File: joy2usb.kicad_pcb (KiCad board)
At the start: 2 copper layers, 55 x 90 mm, 18 parts, among them J1 DB9_Male, J2 Conn_02x04_Odd_Even, SW1 RST, SW2 SW_SPDT, U1 Arduino_Pro_Micro, U2 4066

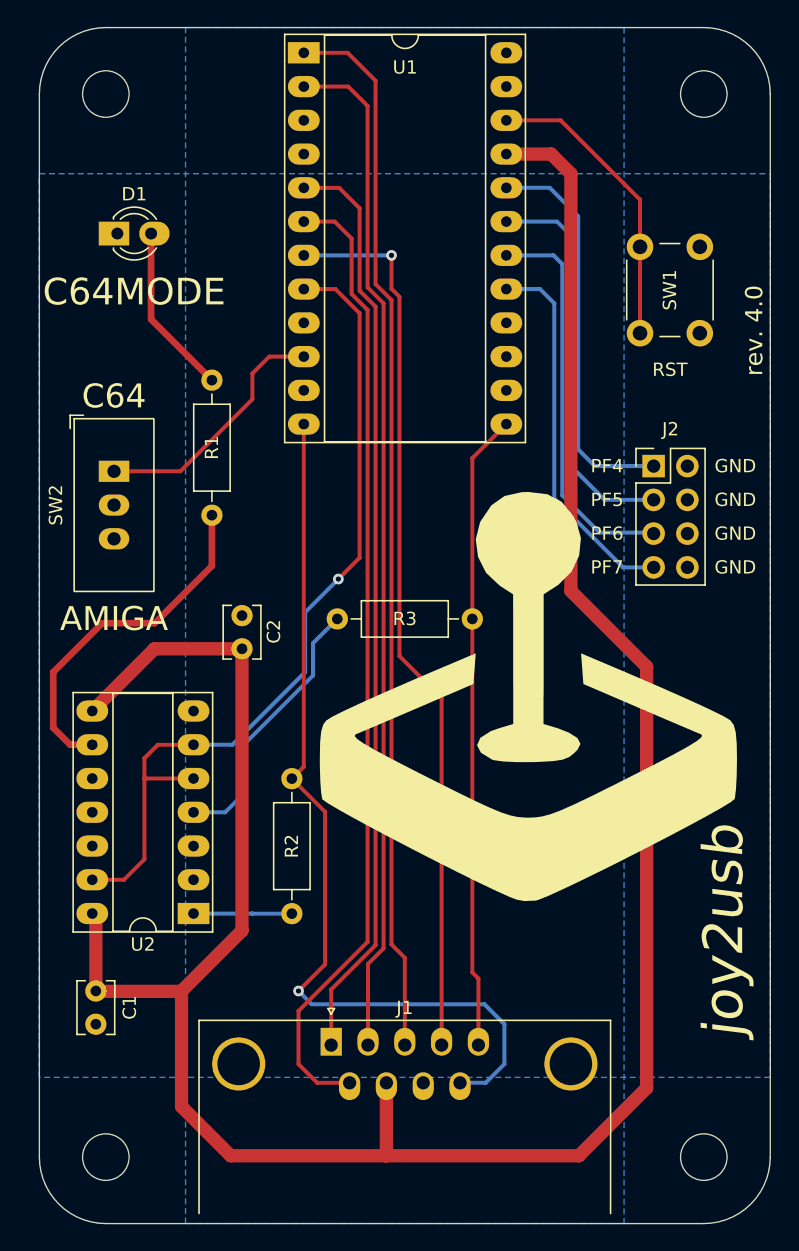
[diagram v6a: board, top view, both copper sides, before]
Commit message: PCB Rev. 4.1
SW2 minor amendment
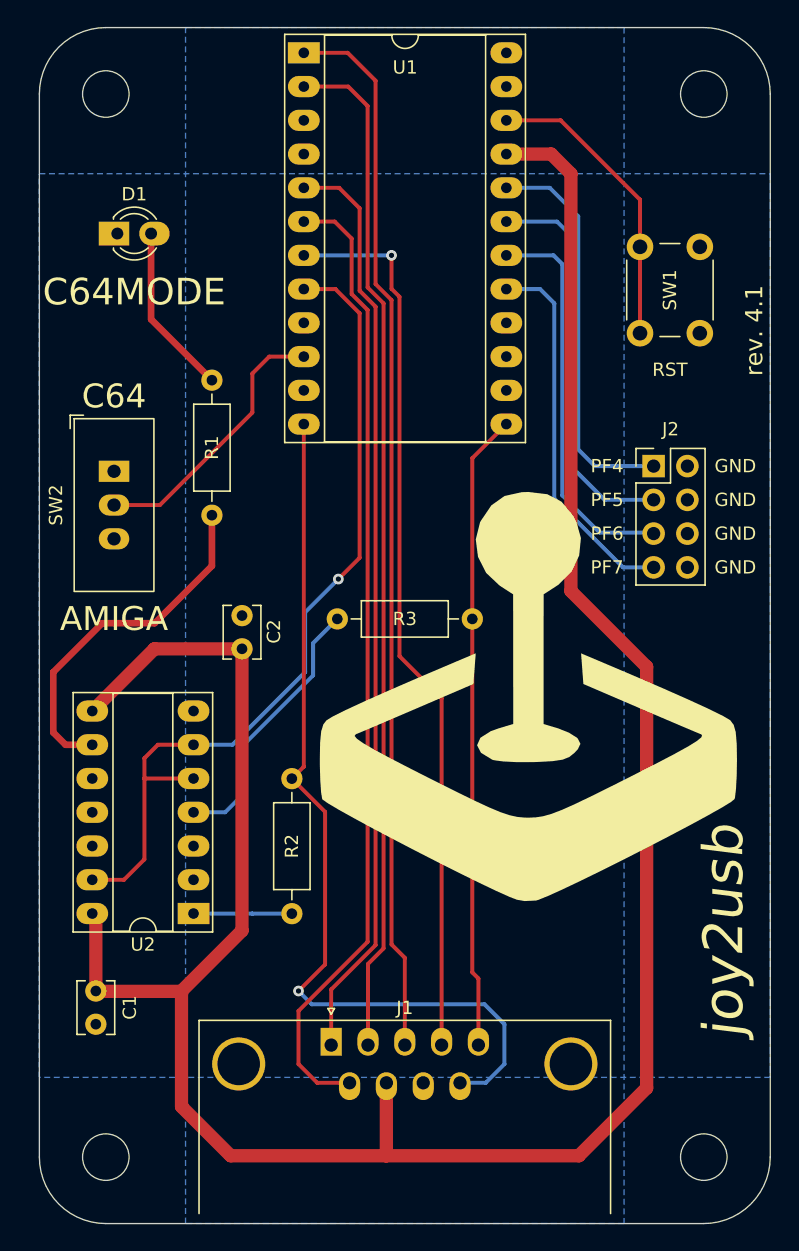
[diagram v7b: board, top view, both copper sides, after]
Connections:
- SW2 pad 1: Net-(SW2-Pad1) -> GND
- SW2 pad 2: GND -> Net-(SW2-Pad2)
- SW2 pad 3: GND -> unconnected-(SW2-Pad3)
- U1 pad 10: Net-(SW2-Pad1) -> Net-(SW2-Pad2)
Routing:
- net Net-(SW2-Pad2): track 0.00 -> 20.6 mm
- net Net-(SW2-Pad1): track 19.0 -> 0.00 mm
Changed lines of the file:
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@@
   (title_block
     (title "joy2usb")
-    (rev "4.0")
+    (rev "4.1")
     (company "mistepien")
   )
@@
   (net 20 "/PF4")
   (net 21 "Net-(D1-Pad2)")
-  (net 22 "Net-(SW2-Pad1)")
+  (net 22 "Net-(SW2-Pad2)")
   (net 23 "/F2F3MODE")
   (net 24 "Net-(R1-Pad1)")
   (net 25 "Net-(R2-Pad2)")
   (net 26 "Net-(R3-Pad1)")
+  (net 27 "unconnected-(SW2-Pad3)")
   (footprint "Resistor_THT:R_Axial_DIN0207_L6.3mm_D2.5mm_P10.16mm_Horizontal" (layer "F.Cu")
     (at 135.42 99.5)
@@
     (fp_line (start -1.27 12.45) (end 1.27 12.45) (layer "F.Fab") (width 0.1))
     (pad "1" thru_hole rect (at 0 8.27) (size 2.3 1.6) (drill 1) (layers *.Cu *.Mask)
-      (net 22 "Net-(SW2-Pad1)") (pinfunction "A") (pintype "passive"))
+      (net 8 "GND") (pinfunction "A") (pintype "passive"))
     (pad "2" thru_hole oval (at 0 10.81) (size 2.3 1.6) (drill 1) (layers *.Cu *.Mask)
-      (net 8 "GND") (pinfunction "B") (pintype "passive"))
+      (net 22 "Net-(SW2-Pad2)") (pinfunction "B") (pintype "passive"))
     (pad "3" thru_hole oval (at 0 13.35) (size 2.3 1.6) (drill 1) (layers *.Cu *.Mask)
-      (net 8 "GND") (pinfunction "C") (pintype "passive"))
+      (net 27 "unconnected-(SW2-Pad3)") (pinfunction "C") (pintype "passive+no_connect"))
   )
   (footprint "Capacitor_THT:C_Disc_D3.8mm_W2.6mm_P2.50mm" (layer "F.Cu")
@@
       (net 14 "unconnected-(U1-Pad9)") (pinfunction "Digital6/PD7") (pintype "bidirectional+no_connect"))
     (pad "10" thru_hole oval locked (at 0 22.86) (size 2.4 1.6) (drill 0.8) (layers *.Cu *.Mask)
-      (net 22 "Net-(SW2-Pad1)") (pinfunction "Digital7/PE6") (pintype "bidirectional"))
+      (net 22 "Net-(SW2-Pad2)") (pinfunction "Digital7/PE6") (pintype "bidirectional"))
     (pad "11" thru_hole oval locked (at 0 25.4) (size 2.4 1.6) (drill 0.8) (layers *.Cu *.Mask)
       (net 12 "unconnected-(U1-Pad11)") (pinfunction "Digital8/PB4") (pintype "bidirectional+no_connect"))
@@
   (segment (start 121.407 76.957) (end 121.407 70.5) (width 0.5) (layer "F.Cu") (net 21))
   (segment (start 125.984 81.534) (end 121.407 76.957) (width 0.5) (layer "F.Cu") (net 21))
-  (segment (start 123.608 88.392) (end 129.03 82.97) (width 0.3) (layer "F.Cu") (net 22))
   (segment (start 130.3 79.76) (end 132.9 79.76) (width 0.3) (layer "F.Cu") (net 22))
-  (segment (start 129.03 82.97) (end 129.03 81.03) (width 0.3) (layer "F.Cu") (net 22))
+  (segment (start 118.618 90.932) (end 122.068 90.932) (width 0.3) (layer "F.Cu") (net 22))
   (segment (start 129.03 81.03) (end 130.3 79.76) (width 0.3) (layer "F.Cu") (net 22))
-  (segment (start 118.618 88.392) (end 123.608 88.392) (width 0.3) (layer "F.Cu") (net 22))
+  (segment (start 129.03 83.97) (end 129.03 81.03) (width 0.3) (layer "F.Cu") (net 22))
+  (segment (start 122.068 90.932) (end 129.03 83.97) (width 0.3) (layer "F.Cu") (net 22))
   (segment (start 120.904 109.982) (end 121.915 108.971) (width 0.3) (layer "F.Cu") (net 23))
   (segment (start 120.909 111.511) (end 120.904 111.506) (width 0.3) (layer "F.Cu") (net 23))
@@
   (segment (start 133 103.5) (end 127.534 108.966) (width 0.3) (layer "B.Cu") (net 23))
   (segment (start 133 99) (end 133 103.5) (width 0.3) (layer "B.Cu") (net 23))
-  (segment (start 116.98 108.971) (end 115.321 108.971) (width 0.5) (layer "F.Cu") (net 24))
-  (segment (start 114.046 107.696) (end 114.046 103.505) (width 0.5) (layer "F.Cu") (net 24))
+  (segment (start 114.046 108.046) (end 114.046 103.505) (width 0.5) (layer "F.Cu") (net 24))
+  (segment (start 114.046 103.505) (end 117.729 99.822) (width 0.5) (layer "F.Cu") (net 24))
+  (segment (start 116.98 108.971) (end 114.971 108.971) (width 0.5) (layer "F.Cu") (net 24))
+  (segment (start 117.729 99.822) (end 121.678 99.822) (width 0.5) (layer "F.Cu") (net 24))
+  (segment (start 114.971 108.971) (end 114.046 108.046) (width 0.5) (layer "F.Cu") (net 24))
   (segment (start 121.678 99.822) (end 125.984 95.516) (width 0.5) (layer "F.Cu") (net 24))
   (segment (start 125.984 95.516) (end 125.984 91.694) (width 0.5) (layer "F.Cu") (net 24))
-  (segment (start 115.321 108.971) (end 114.046 107.696) (width 0.5) (layer "F.Cu") (net 24))
-  (segment (start 117.729 99.822) (end 121.678 99.822) (width 0.5) (layer "F.Cu") (net 24))
-  (segment (start 114.046 103.505) (end 117.729 99.822) (width 0.5) (layer "F.Cu") (net 24))
   (segment (start 129.018 121.68) (end 131.572 121.68) (width 0.3) (layer "B.Cu") (net 25))
   (segment (start 124.6 121.671) (end 129.009 121.671) (width 0.3) (layer "B.Cu") (net 25))

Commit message: PCB Rev. 5.0
Minor update of DB9 socket footprint.
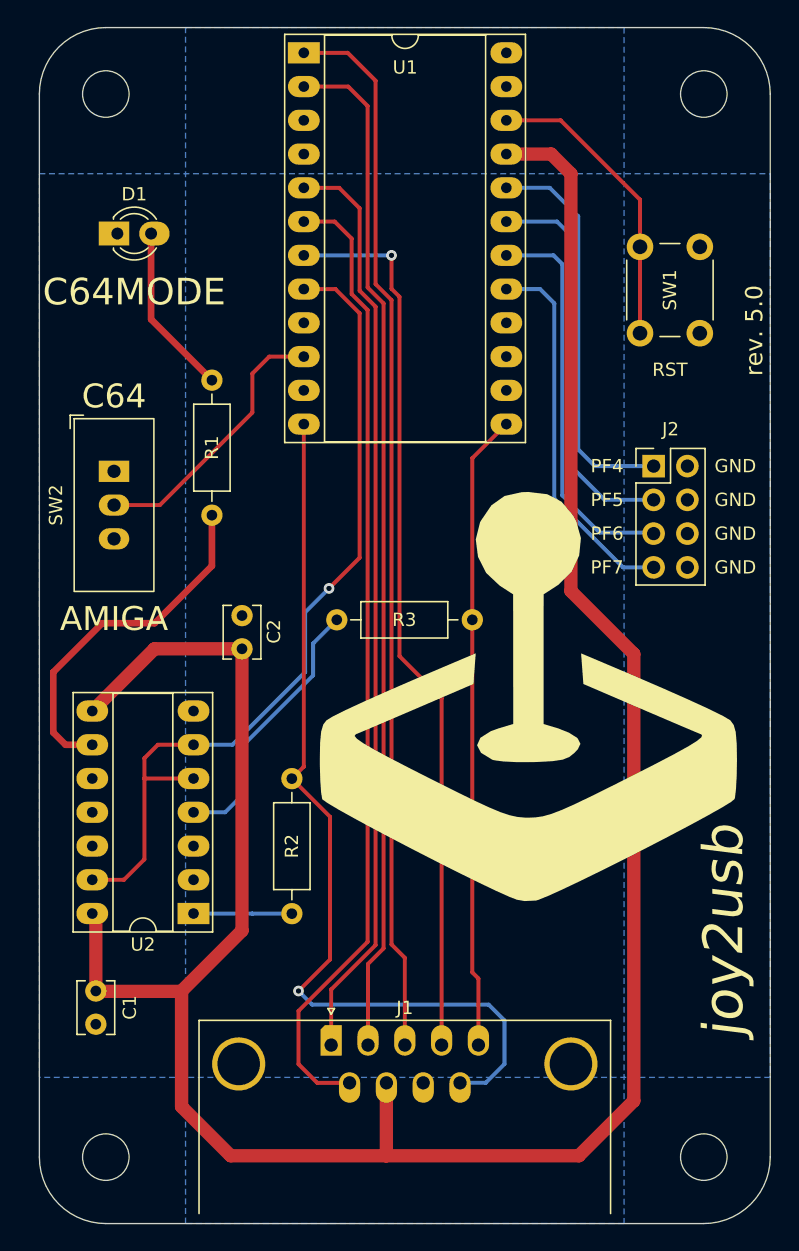
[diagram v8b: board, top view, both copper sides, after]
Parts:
- J1: footprint Misc:DSUB-9_Male_Horizontal_P2.77x2.84mm_EdgePinOffset9.90mm_Housed_OVAL_MountingHolesOffset11.32mm -> misc:DSUB-9_Male_Horizontal_P2.77x2.84mm_EdgePinOffset9.90mm_Housed_OVAL_MountingHolesOffset11.32mm
- moved R3 10.1 mm to (145.5, 99.6), turned to 180 degrees
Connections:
- R3 pad 1: Net-(R3-Pad1) -> /F3BTN
- R3 pad 2: /F3BTN -> Net-(U2-Pad4)
- U2 pad 4: Net-(R3-Pad1) -> Net-(U2-Pad4)
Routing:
- net Net-(R3-Pad1): track 20.4 -> 0.00 mm
- net Net-(U2-Pad4): track 0.00 -> 20.3 mm
- net VCC: track 182.7 -> 181.9 mm
